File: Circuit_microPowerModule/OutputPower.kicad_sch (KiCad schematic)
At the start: 19 parts, among them U1 INA219BxD, U3 MCP4725xxx-xCH, U4 MT3608, U7 MP2315S, U8 LM358

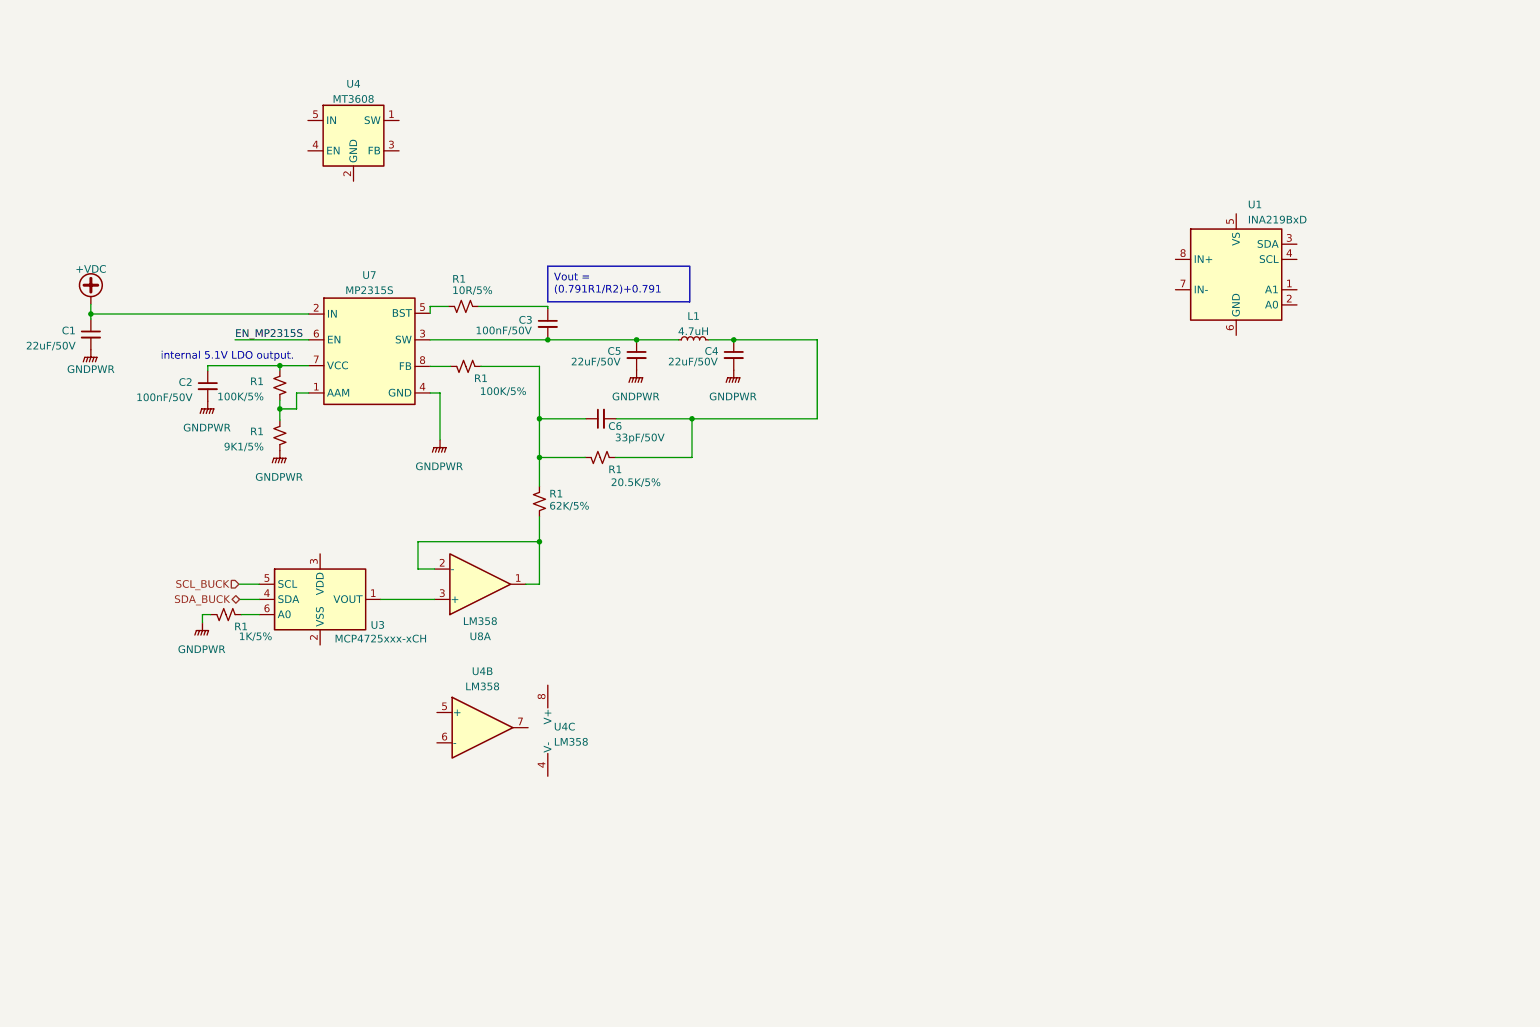
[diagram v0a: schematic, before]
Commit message: added input power OVP circuit
update buck-boost circuit
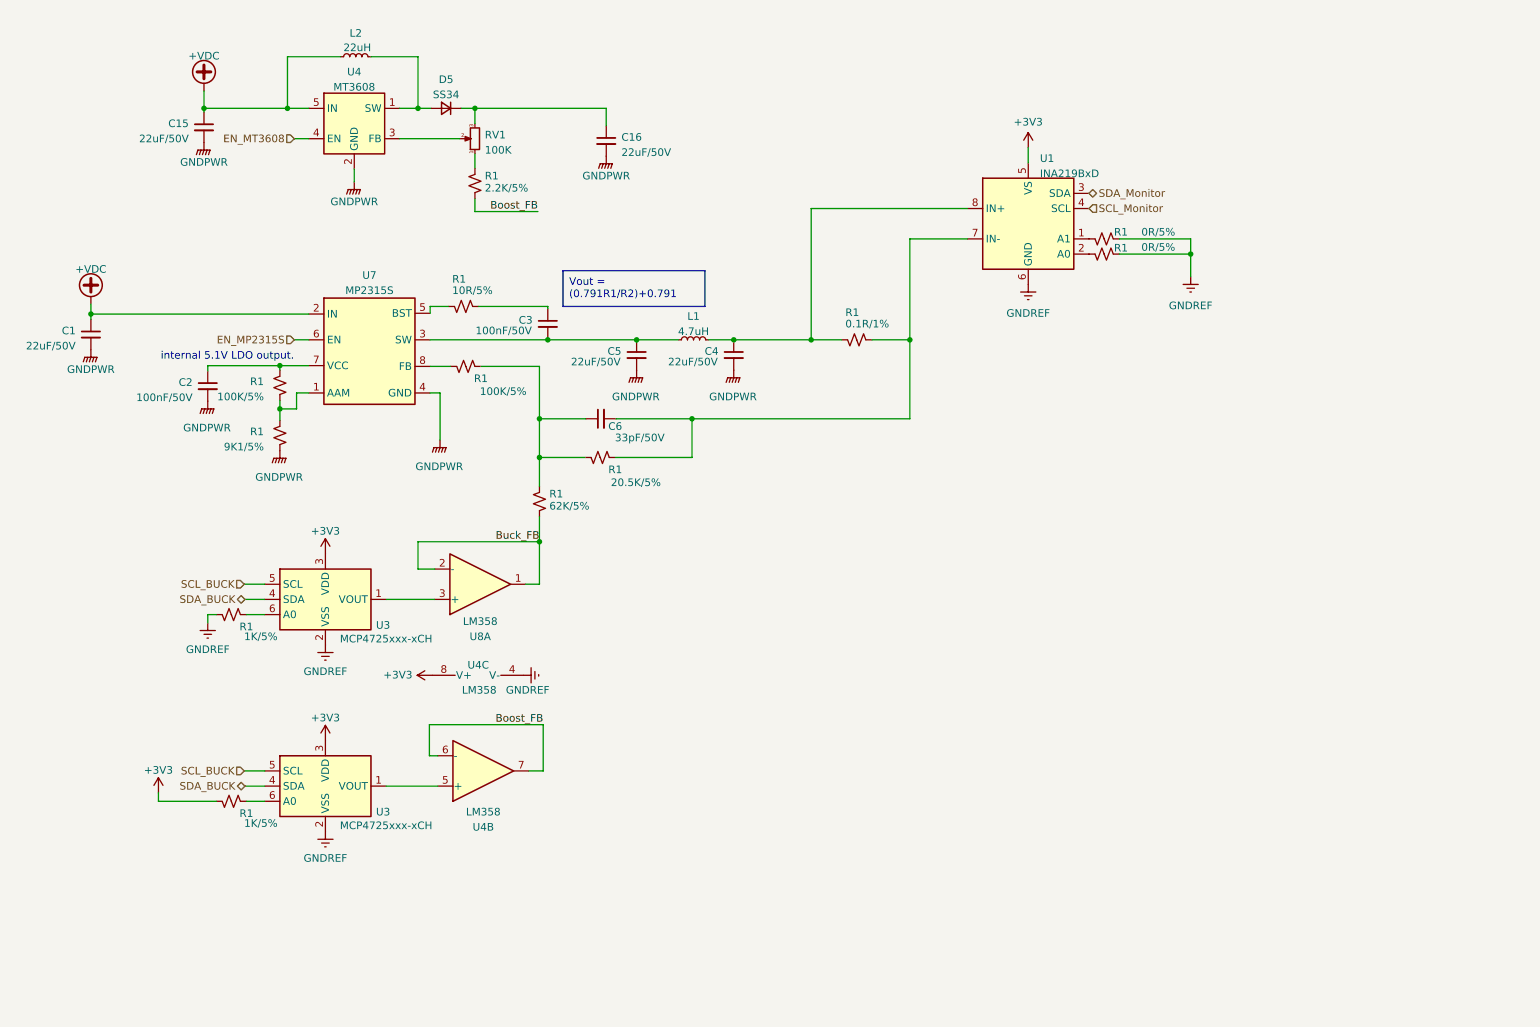
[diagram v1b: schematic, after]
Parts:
- added C15, C16: 22uF/50V, symbol Device:C_Small
- added D5: SS34, symbol Device:D_Small
- added L2: 22uH, symbol Device:L_Small
- added R1 (x2): 0R/5%, Resistor_SMD:R_0603_1608Metric, symbol Device:R_Small_US
- added R1: 1K/5%, Resistor_SMD:R_0603_1608Metric, symbol Device:R_Small_US
- added R1: 0.1R/1%, Resistor_SMD:R_0603_1608Metric, symbol Device:R_Small_US
- added R1: 2.2K/5%, Resistor_SMD:R_0603_1608Metric, symbol Device:R_Small_US
- added RV1: 100K, symbol Device:R_Potentiometer_Small
- added U3: MCP4725xxx-xCH, Package_TO_SOT_SMD:SOT-23-6, symbol Analog_DAC:MCP4725xxx-xCH
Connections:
- net +VDC: now also U4.5 (IN), C15.1, L2.1
- net GNDPWR: now also U4.2 (GND), C15.2, C16.2; no longer R1.2
- net SCL_BUCK: now also U3.5 (SCL)
- net SDA_BUCK: now also U3.4 (SDA)
- net at U1.1 (A1): now also R1.1
- net at U1.2 (A0): now also R1.1
- net SDA_Monitor: now reaches U1.3 (SDA)
- net SCL_Monitor: now reaches U1.4 (SCL)
- net +3V3: now reaches U1.5 (VS)
- net +3V3: now also U3.3 (VDD), U4.8 (V+), R1.2, U3.3 (VDD)
- net GNDREF: now reaches U1.6 (GND)
- net GNDREF: now also R1.2, U3.2 (VSS), U4.4 (V-), R1.2, R1.2, U3.2 (VSS)
- net at U1.7 (IN-): now also C6.2, R1.1, R1.2
- net at U1.8 (IN+): now also C4.1, L1.2, R1.1
- net Buck_FB: now reaches R1.2, U8.1, U8.2 (-)
- net at U4.1 (SW): now also D5.2 (A), L2.2
- net at U4.3 (FB): now also RV1.2
- net EN_MT3608: now reaches U4.4 (EN)
- net at U4.5 (+): now also U3.1 (VOUT)
- net Boost_FB: now reaches U4.6 (-)
- net Boost_FB: now also U4.7, R1.2
- new net: R1.1, U3.6 (A0)
- new net: C16.1, D5.1 (K), RV1.3
- new net: R1.1, RV1.1
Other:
- moved on the sheet: R1, U1, U3, U4, U4B, U4C

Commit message: added boost circuit
create peripheral schematic
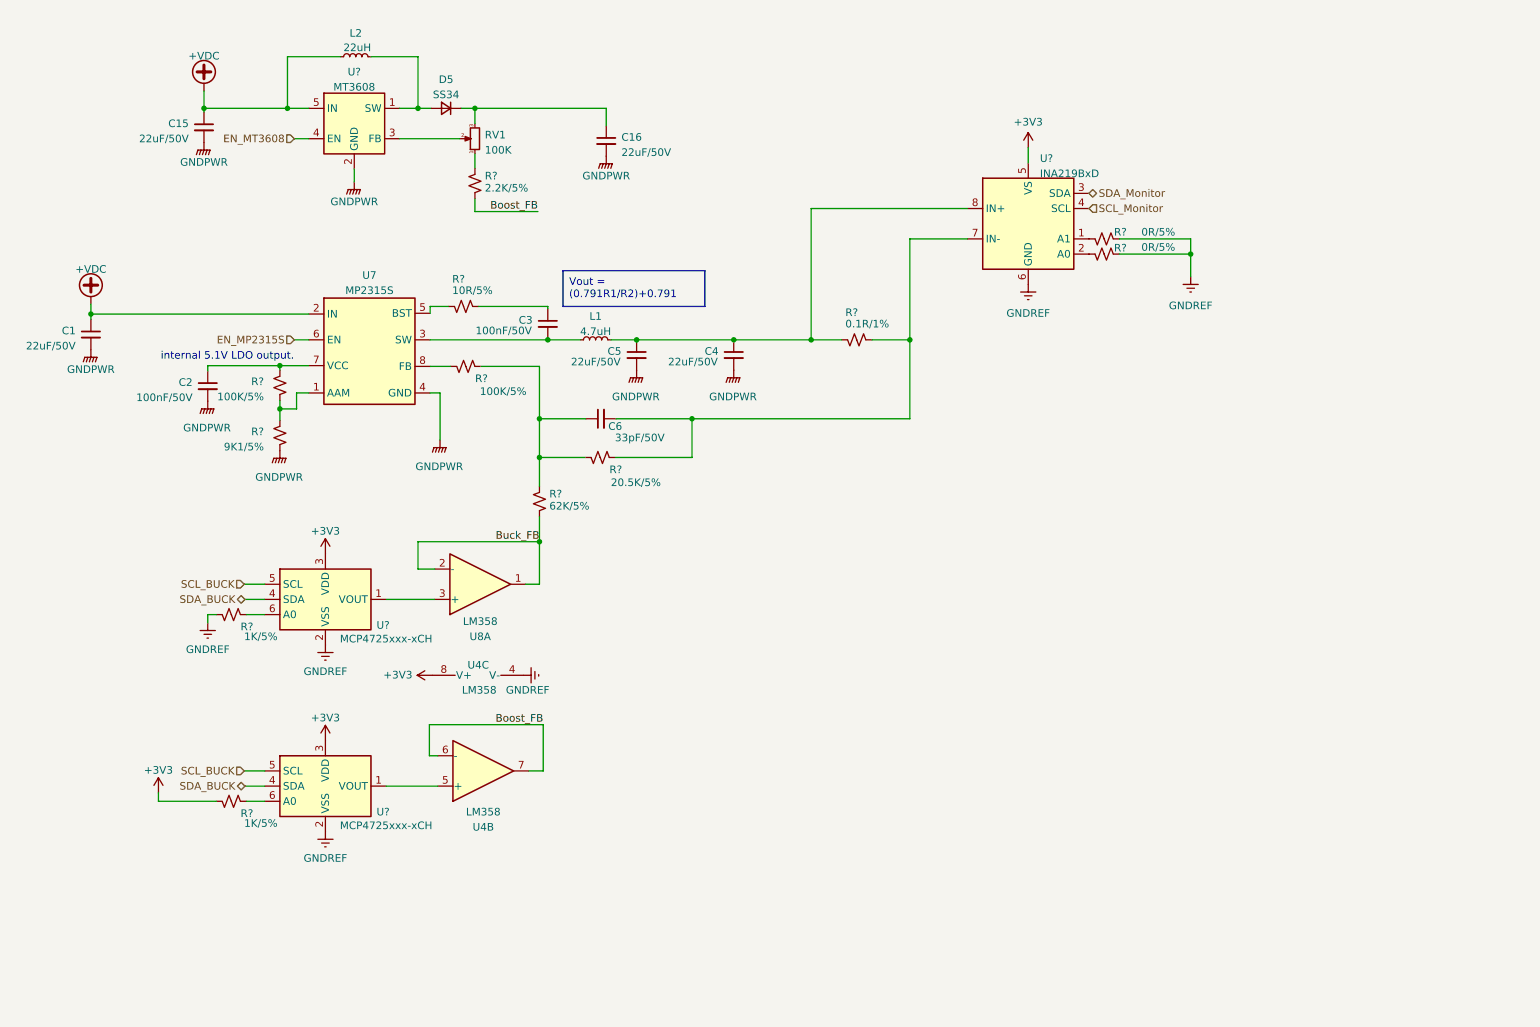
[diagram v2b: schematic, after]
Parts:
- renumbered R1 to R?, U1 to U?, U3 to U?, U4 to U?
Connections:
- net at C4.1, L1.2, R?.1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: now also C5.1
- net at C3.2, L1.1, U7.3 (SW): no longer C5.1
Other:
- moved on the sheet: L1
